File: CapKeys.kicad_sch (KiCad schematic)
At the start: 138 parts, among them J1 USB_C_Receptacle_USB2.0_14P, J10 Conn_01x01, J11 Conn_01x01, J12 Conn_01x01, J13 Conn_01x01, J14 Conn_01x01, J15 Conn_01x01, J16 Conn_01x01, J17 Conn_01x01, J18 Conn_01x01, J19 Conn_01x01, J2 Conn_01x01, J20 Conn_01x01, J21 Conn_01x01, J22 Conn_01x01, J23 Conn_01x01, J24 Conn_01x01, J25 Conn_01x01, J26 Conn_01x01, J27 Conn_01x01, J28 Conn_01x01, J29 Conn_01x01, J3 Conn_01x01, J30 Conn_01x01, J31 Conn_01x01, J32 Conn_01x01, J33 Conn_01x01, J34 Conn_01x01, J35 Conn_01x01, J36 Conn_01x01, J37 Conn_01x01, J38 Conn_01x01, J39 Conn_01x01, J4 Conn_01x01, J40 Conn_01x01, J41 Conn_01x01, J42 Conn_01x01, J43 Conn_01x01, J44 Conn_01x01, J45 Conn_01x01, J46 Conn_01x01, J47 Conn_01x01, J48 Conn_01x01, J5 Conn_01x01, J6 Conn_01x01, J7 Conn_01x01, J8 Conn_01x01, J9 Conn_01x01, U1 AMS1117-3.3, U2 RP2040, U3 W25Q128JVS, U4 MPR121QR2, U5 MPR121QR2, U6 MPR121QR2, U7 MPR121QR2, Y1 X322512MSB4SI

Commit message: Refactor LED sink drive and minor footprint updates
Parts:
- removed D1, D2, D3: KT-0805G, symbol Device:LED
- removed R1, R2, R33, R34, R35, R5: 220R, symbol Device:R
- added D14, D15, D16: GL0805YG01, symbol Device:LED
- added R25, R26, R27, R28, R29, R30: 330R, symbol Device:R
- C22: renamed from C8; value C -> 100n
- C24: renamed from C9; value C -> 100n
- D1: renamed from D4; value KT-0805G -> GL0805YG01
- D10: renamed from D13; value KT-0805G -> GL0805YG01
- D11: renamed from D14; value KT-0805G -> GL0805YG01
- D12: renamed from D15; value KT-0805G -> GL0805YG01
- D13: renamed from D16; value KT-0805G -> GL0805YG01
- D17, D18, D19, D20, D21: value KT-0805G -> GL0805YG01
- D2: renamed from D5; value KT-0805G -> GL0805YG01
- D3: renamed from D6; value KT-0805G -> GL0805YG01
- D4: renamed from D7; value KT-0805G -> GL0805YG01
- D5: renamed from D8; value KT-0805G -> GL0805YG01
- D6: renamed from D9; value KT-0805G -> GL0805YG01
- D7: renamed from D10; value KT-0805G -> GL0805YG01
- D8: renamed from D11; value KT-0805G -> GL0805YG01
- D9: renamed from D12; value KT-0805G -> GL0805YG01
- JP1: renamed from JP2; footprint (none) -> Jumper:SolderJumper-2_P1.3mm_Open_RoundedPad1.0x1.5mm
- JP2: renamed from JP1; footprint (none) -> Jumper:SolderJumper-2_P1.3mm_Open_RoundedPad1.0x1.5mm
- R11: renamed from R6; value 220R -> 330R
- R12: renamed from R9; value 220R -> 330R
- R13: renamed from R20; value 220R -> 330R
- R14: renamed from R21; value 220R -> 330R
- R15: renamed from R22; value 220R -> 330R
- R16: renamed from R23; value 220R -> 330R
- R17: renamed from R24; value 220R -> 330R
- R18: renamed from R25; value 220R -> 330R
- R19: renamed from R26; value 220R -> 330R
- R20: renamed from R27; value 220R -> 330R
- R21: renamed from R28; value 220R -> 330R
- R22: renamed from R29; value 220R -> 330R
- R23: renamed from R30; value 220R -> 330R
- R31, R32: value 220R -> 330R
- U2: renamed from U4; footprint MPR121QR2:QFN40P300X300X60-20N -> Footprints:QFN40P300X300X60-20N
- U4: renamed from U5; footprint MPR121QR2:QFN40P300X300X60-20N -> Footprints:QFN40P300X300X60-20N
- U5: renamed from U6; footprint MPR121QR2:QFN40P300X300X60-20N -> Footprints:QFN40P300X300X60-20N
- U6: renamed from U7; footprint MPR121QR2:QFN40P300X300X60-20N -> Footprints:QFN40P300X300X60-20N
- renumbered C14 to C1, C21 to C10, C22 to C11, C1 to C12, C23 to C13, C24 to C14, C2 to C15, C3 to C16, C4 to C17, C5 to C18, C6 to C19, C17 to C2, C7 to C20, C10 to C21, C11 to C23, C18 to C3, C15 to C4, C16 to C5, C12 to C6, C13 to C7, C19 to C8, C20 to C9, J14 to J11, J18 to J12, J23 to J13, J30 to J14, J37 to J15, J11 to J16, J15 to J17, J19 to J18, J3 to J19, J22 to J2, J5 to J20, J7 to J21, J24 to J22, J31 to J23, J38 to J24, J32 to J26, J39 to J27, J12 to J28, J16 to J29, J29 to J3, J20 to J30, J26 to J31, J33 to J32, J40 to J33, J13 to J34, J17 to J35, J21 to J36, J27 to J37, J34 to J38, J41 to J39, J36 to J4, J46 to J40, J47 to J41, J48 to J42, J28 to J43, J35 to J44, J42 to J45, J43 to J46, J44 to J47, J45 to J48, J2 to J5, J4 to J6, J6 to J7, R15 to R1, R11 to R2, R18 to R24, R12 to R3, R19 to R33, R7 to R34, R8 to R35, R3 to R4, R13 to R5, R16 to R6, R4 to R7, R14 to R8, R17 to R9, U3 to U1, U1 to U3, U2 to U7
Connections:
- net +3V3: now also R31.2, R32.2, R25.2, R26.2, R27.2, R28.2, R29.2, R30.2
- net GND: no longer D17.1 (K), D18.1 (K), D19.1 (K), D20.1 (K), D21.1 (K)
- net LED_OCT1: now also D16.1 (K)
- net LED_OCT2: now also D15.1 (K)
- net LED_OCT3: now also D14.1 (K)
- net LED_PTB+1: now also D20.1 (K); no longer R32.2
- net LED_PTB+2: now also D21.1 (K); no longer R31.2
- net LED_PTB-1: now also D18.1 (K)
- net LED_PTB-2: now also D17.1 (K)
- net LED_PTB0: now also D19.1 (K)
- net at D17.2 (A): now also R28.1; no longer R31.1
- net at D18.2 (A): now also R29.1; no longer R32.1
- net at D19.2 (A): now also R30.1
- net at D20.2 (A): now also R31.1
- net at D21.2 (A): now also R32.1
- new net: D14.2 (A), R25.1
- new net: D15.2 (A), R26.1
- new net: D16.2 (A), R27.1
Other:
- note added: "D14-D21 are driven using current sinking due to RP2040 GPIO current limitations."
- moved on the sheet: C12, C15, C16, C17, C18, C19, C20, C21, C22, C23, C24, D1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

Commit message: Assigned footprints
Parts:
- removed J21: Conn_01x01, symbol Connector_Generic:Conn_01x01
- C1, C10, C11, C12, C13, C14, C15, C16, C17, C18, C19, C2, C20, C21, C22, C23, C24, C3, C4, C5, C6, C7, C8, C9: footprint (none) -> Capacitor_SMD:C_0402_1005Metric
- D1, D10, D11, D12, D13, D14, D15, D16, D17, D18, D19, D2, D20, D21, D3, D4, D5, D6, D7, D8, D9: footprint (none) -> Diode_SMD:D_0805_2012Metric
- J1: value USB_C_Receptacle_USB2.0_14P -> USB_C_Receptacle_USB2.0_16P; footprint (none) -> Connector_USB:USB_C_Receptacle_HCTL_HC-TYPE-C-16P-01A; symbol Connector:USB_C_Receptacle_USB2.0_14P -> Connector:USB_C_Receptacle_USB2.0_16P
- J10, J11, J12, J16, J17, J18: footprint (none) -> Footprints:KEY_BLACK
- J13, J14, J15, J2, J3, J4: footprint (none) -> Footprints:KEY_WHITE
- J19, J20, J5, J6, J7, J8, J9: footprint (none) -> Footprints:KEY_OTHER
- J21: renamed from J22; footprint (none) -> Footprints:KEY_WHITE
- J22: renamed from J23; footprint (none) -> Footprints:KEY_WHITE
- J23: renamed from J24; footprint (none) -> Footprints:KEY_WHITE
- J24: renamed from J25; footprint (none) -> Footprints:KEY_WHITE
- J25: renamed from J26; footprint (none) -> Footprints:KEY_WHITE
- J26: renamed from J27; footprint (none) -> Footprints:KEY_WHITE
- J27: renamed from J28; footprint (none) -> Footprints:KEY_BLACK
- J28: renamed from J29; footprint (none) -> Footprints:KEY_BLACK
- J29: renamed from J30; footprint (none) -> Footprints:KEY_BLACK
- J30: renamed from J31; footprint (none) -> Footprints:KEY_WHITE
- J31: renamed from J32; footprint (none) -> Footprints:KEY_WHITE
- J32: renamed from J33; footprint (none) -> Footprints:KEY_WHITE
- J33: renamed from J34; footprint (none) -> Footprints:KEY_BLACK
- J34: renamed from J35; footprint (none) -> Footprints:KEY_BLACK
- J35: renamed from J36; footprint (none) -> Footprints:KEY_BLACK
- J36: renamed from J37; footprint (none) -> Footprints:KEY_WHITE
- J37: renamed from J38; footprint (none) -> Footprints:KEY_WHITE
- J38: renamed from J39; footprint (none) -> Footprints:KEY_WHITE
- J39: renamed from J40; footprint (none) -> Footprints:KEY_BLACK
- J40: renamed from J41; footprint (none) -> Footprints:KEY_BLACK
- J41: renamed from J42; footprint (none) -> Footprints:KEY_BLACK
- J42: renamed from J43; footprint (none) -> Footprints:KEY_WHITE
- J43: renamed from J44; footprint (none) -> Footprints:KEY_WHITE
- J44: renamed from J45; footprint (none) -> Footprints:KEY_WHITE
- J45: renamed from J46; footprint (none) -> Footprints:KEY_WHITE
- J46: renamed from J47; footprint (none) -> Footprints:KEY_WHITE
- J47: renamed from J48; footprint (none) -> Footprints:KEY_WHITE
- R1, R10, R11, R12, R13, R14, R15, R16, R17, R18, R19, R2, R20, R21, R22, R23, R24, R25, R26, R27, R28, R29, R3, R30, R31, R32, R33, R34, R35, R4, R5, R6, R7, R8, R9: footprint (none) -> Resistor_SMD:R_0402_1005Metric
- Y1: footprint (none) -> Crystal:Crystal_SMD_3225-4Pin_3.2x2.5mm
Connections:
- no-connect marks 9 -> 11

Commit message: Updated symbols and footprints
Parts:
- removed J10, J11, J12, J16, J17, J18, J27, J28, J29, J33, J34, J35, J39, J40, J41: Conn_01x01, Footprints:KEY_BLACK, symbol Connector_Generic:Conn_01x01
- removed J13, J14, J15, J2, J21, J22, J23, J24, J25, J26, J3, J30, J31, J32, J36, J37, J38, J4, J42, J43, J44, J45, J46, J47: Conn_01x01, Footprints:KEY_WHITE, symbol Connector_Generic:Conn_01x01
- removed J5, J6, J7, J8, J9: Conn_01x01, Footprints:KEY_OTHER, symbol Connector_Generic:Conn_01x01
- added U8: (no value), symbol keys:piano_keys
- added U9: (no value), symbol Symbols:pitch_bend
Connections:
- net KEY_A#_1: now also U8.31 (A#1)
- net KEY_A#_2: now also U8.32 (A#2)
- net KEY_A#_3: now also U8.33 (A#3)
- net KEY_A_1: now also U8.28 (A1)
- net KEY_A_2: now also U8.29 (A2)
- net KEY_A_3: now also U8.30 (A3)
- net KEY_B_1: now also U8.34 (B1)
- net KEY_B_2: now also U8.35 (B2)
- net KEY_B_3: now also U8.36 (B3)
- net KEY_C#_1: now also U8.4 (C#1)
- net KEY_C#_2: now also U8.5 (C#2)
- net KEY_C#_3: now also U8.6 (C#3)
- net KEY_C_1: now also U8.1 (C1)
- net KEY_C_2: now also U8.2 (C2)
- net KEY_C_3: now also U8.3 (C3)
- net KEY_D#_1: now also U8.10 (D#1)
- net KEY_D#_2: now also U8.11 (D#2)
- net KEY_D#_3: now also U8.12 (D#3)
- net KEY_D_1: now also U8.7 (D1)
- net KEY_D_2: now also U8.8 (D2)
- net KEY_D_3: now also U8.9 (D3)
- net KEY_E_1: now also U8.13 (E1)
- net KEY_E_2: now also U8.14 (E2)
- net KEY_E_3: now also U8.15 (E3)
- net KEY_F#_1: now also U8.19 (F#1)
- net KEY_F#_2: now also U8.20 (F#2)
- net KEY_F#_3: now also U8.21 (F#3)
- net KEY_F_1: now also U8.16 (F1)
- net KEY_F_2: now also U8.17 (F2)
- net KEY_F_3: now also U8.18 (F3)
- net KEY_G#_1: now also U8.25 (G#1)
- net KEY_G#_2: now also U8.26 (G#2)
- net KEY_G#_3: now also U8.27 (G#3)
- net KEY_G_1: now also U8.22 (G1)
- net KEY_G_2: now also U8.23 (G2)
- net KEY_G_3: now also U8.24 (G3)
- net KEY_HC_1: now also U8.37 (HC1)
- net KEY_HC_2: now also U8.38 (HC2)
- net KEY_HC_3: now also U8.39 (HC3)
- net KEY_PTB+1: now also U9.2 (PTB+1)
- net KEY_PTB+2: now also U9.1 (PTB+2)
- net KEY_PTB-1: now also U9.4 (PTB-1)
- net KEY_PTB-2: now also U9.5 (PTB-2)
- net KEY_PTB0: now also U9.3 (PTB0)
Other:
- moved on the sheet: J19, J20, JP1, JP2, R1, R2, R3, R5, R8

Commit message: Added mounting holes
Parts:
- added H1, H2, H3, H4, H5, H6: MountingHole, symbol Mechanical:MountingHole
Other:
- note added: "MOUNTING HOLES"
- note added: "RESET BOOT"
- note removed: "RESET_BOOT"

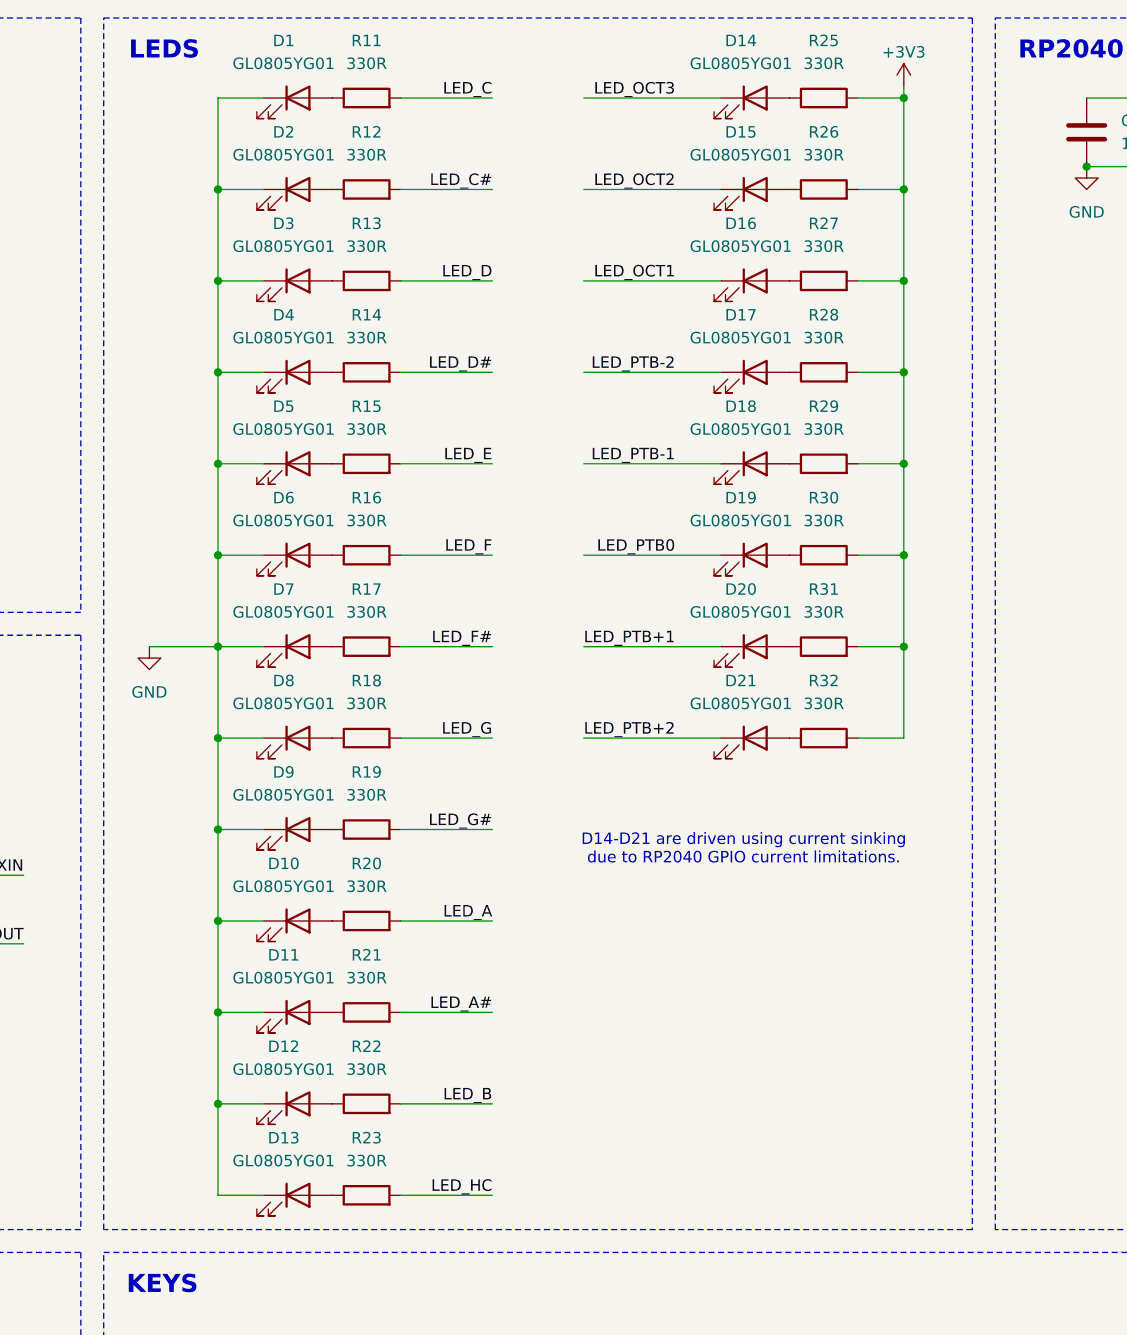
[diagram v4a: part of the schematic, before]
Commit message: Updated footprints,symbols,and PCB
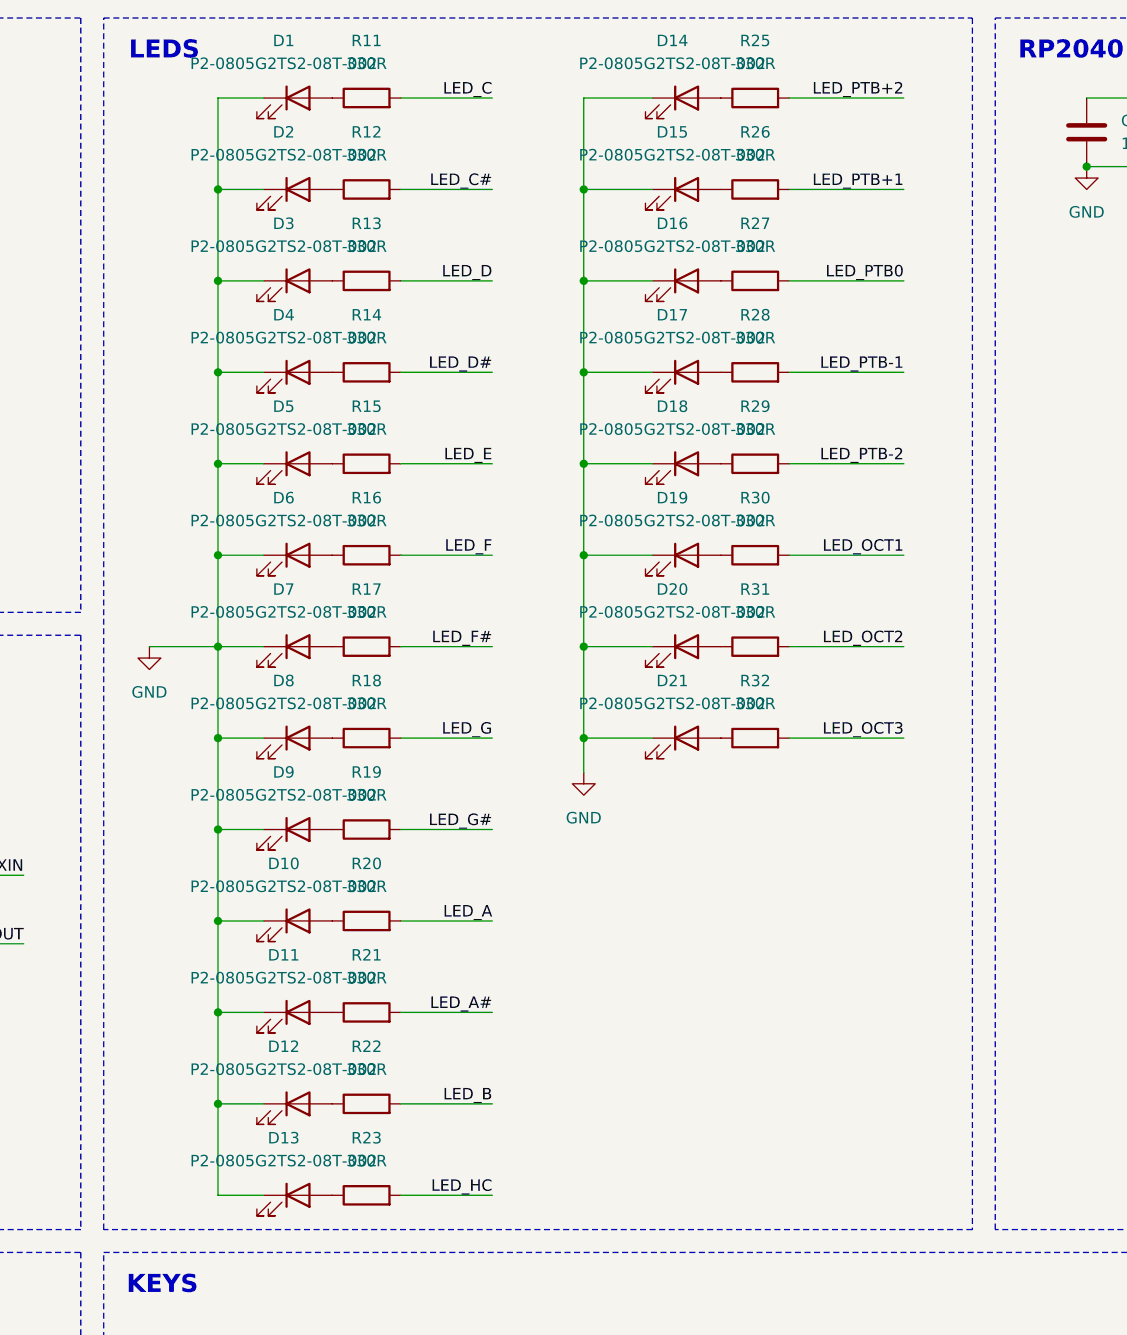
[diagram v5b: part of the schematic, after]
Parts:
- C6, C7: footprint Capacitor_SMD:C_0402_1005Metric -> Capacitor_SMD:C_1206_3216Metric
- D1, D10, D11, D12, D13, D14, D15, D16, D17, D18, D19, D2, D20, D21, D3, D4, D5, D6, D7, D8, D9: value GL0805YG01 -> P2-0805G2TS2-08T-002
- H1, H2, H3, H4, H5, H6: footprint (none) -> MountingHole:MountingHole_3.2mm_M3
- U8: footprint (none) -> Footprints:KEYS
- U9: footprint (none) -> Footprints:PTB_KEYS
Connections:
- net +3V3: no longer R25.2, R26.2, R27.2, R28.2, R29.2, R30.2, R31.2, R32.2
- net GND: now also D14.1 (K), D15.1 (K), D16.1 (K), D17.1 (K), D18.1 (K), D19.1 (K), D20.1 (K), D21.1 (K)
- net LED_OCT1: now also R30.2; no longer D16.1 (K)
- net LED_OCT2: now also R31.2; no longer D15.1 (K)
- net LED_OCT3: now also R32.2; no longer D14.1 (K)
- net LED_PTB+1: now also R26.2; no longer D20.1 (K)
- net LED_PTB+2: now also R25.2; no longer D21.1 (K)
- net LED_PTB-1: now also R28.2; no longer D18.1 (K)
- net LED_PTB-2: now also R29.2; no longer D17.1 (K)
- net LED_PTB0: now also R27.2; no longer D19.1 (K)
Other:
- note removed: "D14-D21 are driven using current sinking due to RP2040 GPIO current limitations."
- moved on the sheet: D14, D15, D16, D17, D18, D19, D20, D21, R25, R26, R27, R28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

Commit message: Updated PCB and schematic
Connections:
- net KEY_A#_1: now also U6.9 (ELEC1); no longer U2.18 (ELEC10)
- net KEY_A#_2: now also U6.10 (ELEC2); no longer U4.18 (ELEC10)
- net KEY_A#_3: now also U6.11 (ELEC3); no longer U5.18 (ELEC10)
- net KEY_A_1: now also U5.18 (ELEC10); no longer U2.17 (ELEC9)
- net KEY_A_2: now also U5.19 (ELEC11); no longer U4.17 (ELEC9)
- net KEY_A_3: now also U6.8 (ELEC0); no longer U5.17 (ELEC9)
- net KEY_B_1: now also U6.12 (ELEC4); no longer U2.19 (ELEC11)
- net KEY_B_2: now also U6.13 (ELEC5); no longer U4.19 (ELEC11)
- net KEY_B_3: now also U6.14 (ELEC6); no longer U5.19 (ELEC11)
- net KEY_C#_1: now also U2.18 (ELEC10); no longer U2.9 (ELEC1)
- net KEY_C#_2: now also U2.19 (ELEC11); no longer U4.9 (ELEC1)
- net KEY_C#_3: now also U4.8 (ELEC0); no longer U5.9 (ELEC1)
- net KEY_C_1: now also U2.15 (ELEC7); no longer U2.8 (ELEC0)
- net KEY_C_2: now also U2.16 (ELEC8); no longer U4.8 (ELEC0)
- net KEY_C_3: now also U2.17 (ELEC9); no longer U5.8 (ELEC0)
- net KEY_D#_1: now also U4.12 (ELEC4); no longer U2.11 (ELEC3)
- net KEY_D#_2: now also U4.13 (ELEC5); no longer U4.11 (ELEC3)
- net KEY_D#_3: now also U4.14 (ELEC6); no longer U5.11 (ELEC3)
- net KEY_D_1: now also U4.9 (ELEC1); no longer U2.10 (ELEC2)
- net KEY_D_3: now also U4.11 (ELEC3); no longer U5.10 (ELEC2)
- net KEY_E_1: now also U4.15 (ELEC7); no longer U2.12 (ELEC4)
- net KEY_E_2: now also U4.16 (ELEC8); no longer U4.12 (ELEC4)
- net KEY_E_3: now also U4.17 (ELEC9); no longer U5.12 (ELEC4)
- net KEY_F#_1: now also U5.9 (ELEC1); no longer U2.14 (ELEC6)
- net KEY_F#_2: now also U5.10 (ELEC2); no longer U4.14 (ELEC6)
- net KEY_F#_3: now also U5.11 (ELEC3); no longer U5.14 (ELEC6)
- net KEY_F_1: now also U4.18 (ELEC10); no longer U2.13 (ELEC5)
- net KEY_F_2: now also U4.19 (ELEC11); no longer U4.13 (ELEC5)
- net KEY_F_3: now also U5.8 (ELEC0); no longer U5.13 (ELEC5)
- net KEY_G#_1: now also U5.15 (ELEC7); no longer U2.16 (ELEC8)
- net KEY_G#_2: now also U5.16 (ELEC8); no longer U4.16 (ELEC8)
- net KEY_G#_3: now also U5.17 (ELEC9); no longer U5.16 (ELEC8)
- net KEY_G_1: now also U5.12 (ELEC4); no longer U2.15 (ELEC7)
- net KEY_G_2: now also U5.13 (ELEC5); no longer U4.15 (ELEC7)
- net KEY_G_3: now also U5.14 (ELEC6); no longer U5.15 (ELEC7)
- net KEY_HC_1: now also U6.15 (ELEC7); no longer U6.8 (ELEC0)
- net KEY_HC_2: now also U6.16 (ELEC8); no longer U6.9 (ELEC1)
- net KEY_HC_3: now also U6.17 (ELEC9); no longer U6.10 (ELEC2)
- net KEY_OCT+: now also U2.8 (ELEC0); no longer U6.11 (ELEC3)
- net KEY_OCT-: now also U2.9 (ELEC1); no longer U6.12 (ELEC4)
- net KEY_PTB+1: now also U2.11 (ELEC3); no longer U6.14 (ELEC6)
- net KEY_PTB+2: now also U2.12 (ELEC4); no longer U6.15 (ELEC7)
- net KEY_PTB-1: now also U2.13 (ELEC5); no longer U6.16 (ELEC8)
- net KEY_PTB-2: now also U2.14 (ELEC6); no longer U6.17 (ELEC9)
- net KEY_PTB0: now also U2.10 (ELEC2); no longer U6.13 (ELEC5)
- net KEY_MUTE: no longer names the net of U6.18 (ELEC10)
- no-connect marks 11 -> 12

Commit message: Updated PCB
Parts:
- removed H3, H4, H5, H6: MountingHole, MountingHole:MountingHole_3.2mm_M3, symbol Mechanical:MountingHole

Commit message: Updated PCB and Footprints
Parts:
- U2, U4, U5, U6: footprint Footprints:QFN40P300X300X60-20N -> Package_DFN_QFN:UQFN-20_3x3mm_P0.4mm
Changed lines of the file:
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@@
 			)
 		)
-		(property "Footprint" "Footprints:QFN40P300X300X60-20N"
+		(property "Footprint" "Package_DFN_QFN:UQFN-20_3x3mm_P0.4mm"
 			(at 57.15 254 0)
 			(hide yes)
@@
 			)
 		)
-		(property "Footprint" "Footprints:QFN40P300X300X60-20N"
+		(property "Footprint" "Package_DFN_QFN:UQFN-20_3x3mm_P0.4mm"
 			(at 123.19 254 0)
 			(hide yes)
@@
 			)
 		)
-		(property "Footprint" "Footprints:QFN40P300X300X60-20N"
+		(property "Footprint" "Package_DFN_QFN:UQFN-20_3x3mm_P0.4mm"
 			(at 187.96 254 0)
 			(hide yes)
@@
 			)
 		)
-		(property "Footprint" "Footprints:QFN40P300X300X60-20N"
+		(property "Footprint" "Package_DFN_QFN:UQFN-20_3x3mm_P0.4mm"
 			(at 252.73 254 0)
 			(hide yes)
